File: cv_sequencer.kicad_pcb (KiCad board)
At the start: 4 copper layers, 111.3 x 22.4 mm, 110 parts, among them J1 4027_Connector_PicoBlade_3pos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, J10 3085_MiniJack_Thonk_Vert, J11 3085_MiniJack_Thonk_Vert, J12 3085_MiniJack_Thonk_Vert, J13 3085_MiniJack_Thonk_Vert, J2 4005_SWD_Header, J3 3086_Connector_Eurorack_Power, J4 3096_USBC_RA_SMD, J5 CV_OFFSET, J6 3085_MiniJack_Thonk_Vert, J7 3085_MiniJack_Thonk_Vert, J8 3085_MiniJack_Thonk_Vert, J9 3085_MiniJack_Thonk_Vert, SW1 RST, SW2 BOOTSEL, U1 3097_TFT_Display_SPI, U2 4002_RP2040, U3 4015_Adjustable_Reg_500mA_SOT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, U4 4015_Adjustable_Reg_500mA_SOT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, U5 4014_Voltage_Reference_5V_SOT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, U6 4001_MCP48FEB24_DAC, U7 3099_TL074CPW_SMD, U8 3099_TL074CPW_SMD, Y1 4004-Crystal-12MHz_GND24

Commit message: Made minor tweaks, started routing of board
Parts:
- added R31: 4030_Resistor_SMD_220_0.125W_1%, Shulltronics_Generics:RES-0402, B.Cu at (137.6, 77.9)
- added R32: 4008_Resistor_SMD_10k_0.125W_1%, Shulltronics_Generics:RES-0402, B.Cu at (145.3, 70.5)
- added R33: 4030_Resistor_SMD_220_0.125W_1%, Shulltronics_Generics:RES-0402, B.Cu at (136.4, 77.9)
- added U9: 4028_OptoIsolator_TLP290, Shulltronics_Opto:4028_OptoIsolator_TLP290_SOP-4, B.Cu at (140.8, 74.9)
- C13, C15, C16, C17: value 4013_Capacitor_1u_16V_0402 -> 4035_Capacitor_2u2_25V_0402
- C20, C21: value 3088_Capacitor_10u_50V_SMD -> 4031_Capacitor_10u_35V_SMD
- J1: value 4027_Connector_PicoBlade_3pos_Vert_THT -> 4029_Connector_PicoBlade_4pos_Vert_THT; footprint Shulltronics_Connectors:4027_PicoBlade_3pos_Vert_THT -> Shulltronics_Connectors:4029_PicoBlade_4pos_Vert_THT
- R10: value 4020_Resistor_SMD_180k_0.125W_1% -> 4033_Resistor_SMD_18k_0.125W_1%
- R11, R9: value 4019_Resistor_SMD_270k_0.125W_1% -> 4016_Resistor_SMD_27k_0.125W_1%
- R12: value 4018_Resistor_SMD_82k_0.125W_1% -> 4034_Resistor_SMD_8k2_0.125W_1%
- TP11, TP12, TP15, TP16, TP18: moved to F.Cu
- U3, U4: value 4015_Adjustable_Reg_500mA_SOT-23-5 -> 4032_Adjustable_Reg_200mA_SOT-23-5
- moved TP11 95.7 mm to (138.5, 85.4), turned to 0 degrees
- moved TP15 89.5 mm to (131.2, 85.3), turned to 0 degrees
- moved TP12 89.3 mm to (141.6, 85.4), turned to 0 degrees
- moved TP16 89.0 mm to (128.1, 85.3), turned to 0 degrees
- moved TP18 88.6 mm to (125.0, 85.3), turned to 0 degrees
- moved TP28 41.1 mm to (165.6, 85.3)
- moved TP29 39.7 mm to (168.7, 85.3)
- moved R24 37.8 mm to (172.8, 75.1)
- moved R27 37.3 mm to (172.8, 77.6), turned to 180 degrees
- moved R23 35.4 mm to (172.8, 76.4), turned to 0 degrees
- moved R1 35.2 mm to (146.6, 70.5), turned to -90 degrees
- moved R28 35.0 mm to (172.8, 73.8), turned to 0 degrees
- moved TP19 31.2 mm to (168.9, 66.0)
- moved TP20 31.2 mm to (175.1, 66.0)
- moved TP22 28.0 mm to (165.8, 66.0)
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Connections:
- net Net-(J5-Pad2) renamed /IO Jacks/CVx_REF
- C22 pad 2: /IO Jacks/5V3 -> /5V3
- C8 pad 2: /XOUT -> Net-(C8-Pad2)
- J1 pad 1: unconnected-(J1-Pad1) -> /MIDI_SNK
- J1 pad 2: unconnected-(J1-Pad2) -> /MIDI_SRC
- J1 pad 3: unconnected-(J1-Pad3) -> /UART_TX
- R10 pad 1: GND -> Net-(R9-Pad2)
- R10 pad 2: Net-(R10-Pad2) -> GND
- R11 pad 1: Net-(R11-Pad1) -> /5V3
- R11 pad 2: /5V3 -> Net-(R11-Pad2)
- R12 pad 1: GND -> Net-(R11-Pad2)
- R12 pad 2: Net-(R11-Pad1) -> GND
- R4 pad 1: /XOUT -> Net-(C8-Pad2)
- R4 pad 2: Net-(R4-Pad2) -> /XOUT
- R9 pad 1: Net-(R10-Pad2) -> VCC
- R9 pad 2: VCC -> Net-(R9-Pad2)
- U2 pad 21: Net-(R4-Pad2) -> /XOUT
- U3 pad 4: Net-(R10-Pad2) -> Net-(R9-Pad2)
- U4 pad 4: Net-(R11-Pad1) -> Net-(R11-Pad2)
- U5 pad 3: /IO Jacks/5V3 -> /5V3
- U6 pad 2: /IO Jacks/5V3 -> /5V3
- Y1 pad 3: /XOUT -> Net-(C8-Pad2)
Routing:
- net VSS: track 0.00 -> 105.3 mm, vias 0 -> 3
- net VDD: track 0.00 -> 100.9 mm, vias 0 -> 3
- net /~{RESET}: track 0.00 -> 47.5 mm, vias 0 -> 4
- net /IO Jacks/TRIG0: track 0.00 -> 35.3 mm
- net /IO Jacks/CV3_OUT: track 0.00 -> 32.3 mm
- net /IO Jacks/CV0_OUT: track 0.00 -> 26.9 mm
- net GND: track 0.00 -> 24.5 mm, vias 0 -> 28
- net /SWCLK: track 0.00 -> 23.8 mm, vias 0 -> 2
- net /SWDIO: track 0.00 -> 22.6 mm, vias 0 -> 2
- net /IO Jacks/DAC_VOUT3: track 0.00 -> 21.5 mm, vias 0 -> 2
- net /IO Jacks/DAC_VOUT1: track 0.00 -> 18.6 mm, vias 0 -> 2
- net /IO Jacks/TRIG1: track 0.00 -> 18.4 mm
- net VCC: track 0.00 -> 16.6 mm, vias 0 -> 15
- net /IO Jacks/DAC_VOUT2: track 0.00 -> 16.0 mm, vias 0 -> 2
- net /IO Jacks/DAC_VOUT0: track 0.00 -> 14.3 mm, vias 0 -> 2
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- added copper zone on B.Cu, net GND
- added copper zone on In2.Cu, net GND
- added copper zone on F.Cu, net VCC
- added copper zone on B.Cu, net VDD
- added copper zone on B.Cu, net VSS

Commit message: some more routing
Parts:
- removed TP1: ENC_BTN, Shulltronics_Generics:TestPoint_Pad_D2.0mm
- removed TP2: LCD/SD_SCK, Shulltronics_Generics:TestPoint_Pad_D2.0mm
- removed TP21: DAC_VOUT0, Shulltronics_Generics:TestPoint_Pad_D2.0mm
- removed TP25: DAC_VOUT2, Shulltronics_Generics:TestPoint_Pad_D2.0mm
- removed TP26: DAC_VOUT3, Shulltronics_Generics:TestPoint_Pad_D2.0mm
- removed TP29: TRIG1, Shulltronics_Generics:TestPoint_Pad_D2.0mm
- removed TP3: SD_SDO, Shulltronics_Generics:TestPoint_Pad_D2.0mm
- removed TP30: TRIG2, Shulltronics_Generics:TestPoint_Pad_D2.0mm
- removed TP31: TRIG3, Shulltronics_Generics:TestPoint_Pad_D2.0mm
- removed TP4: LCD/SD_SDI, Shulltronics_Generics:TestPoint_Pad_D2.0mm
- removed TP5: LCD_CS, Shulltronics_Generics:TestPoint_Pad_D2.0mm
- removed TP6: LCD_RST, Shulltronics_Generics:TestPoint_Pad_D2.0mm
- removed TP7: LCD_DC, Shulltronics_Generics:TestPoint_Pad_D2.0mm
- removed TP8: SD_CS, Shulltronics_Generics:TestPoint_Pad_D2.0mm
- moved TP24 26.5 mm to (174.5, 66.0)
- moved TP23 9.91 mm to (162.1, 66.0)
- moved TP20 9.91 mm to (165.2, 66.0)
- moved R17 9.02 mm to (193.9, 80.5), turned to 180 degrees
- moved R18 7.19 mm to (196.5, 72.3)
- moved R22 7.19 mm to (194.3, 72.3)
- moved R21 6.67 mm to (193.9, 79.2), turned to 0 degrees
- moved C10 3.30 mm to (155.3, 71.1), turned to 90 degrees
- moved TP28 3.25 mm to (162.3, 85.3)
- moved TP19 2.49 mm to (171.4, 66.0)
- moved TP22 2.49 mm to (168.3, 66.0)
- moved R2 1.37 mm to (154.9, 66.8)
- moved R3 1.27 mm to (154.9, 68.2)
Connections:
- U2 pad 38: /IO_TRIG0 -> /IO_TRIG3
- U2 pad 41: /IO_TRIG3 -> /IO_TRIG0
- U8 pad 10: /IO Jacks/TRIG2 -> /IO Jacks/TRIG3
- U8 pad 12: /IO Jacks/TRIG3 -> /IO Jacks/TRIG2
- U8 pad 13: /IO Jacks/TRIG3_FB -> /IO Jacks/TRIG2_FB
- U8 pad 14: /IO Jacks/TRIG3_FB -> /IO Jacks/TRIG2_FB
- U8 pad 8: /IO Jacks/TRIG2_FB -> /IO Jacks/TRIG3_FB
- U8 pad 9: /IO Jacks/TRIG2_FB -> /IO Jacks/TRIG3_FB
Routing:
- net /5V3: track 5.44 -> 72.8 mm, vias 0 -> 2
- net /IO_TRIG0: track 0.00 -> 46.3 mm, vias 0 -> 3
- net /IO_TRIG3: track 2.64 -> 45.7 mm, vias 0 -> 2
- net /IO_TRIG2: track 1.67 -> 43.5 mm, vias 0 -> 3
- net /ENC_1: track 0.00 -> 40.3 mm, vias 0 -> 2
- net /ENC_BTN: track 5.93 -> 41.4 mm, vias 0 -> 3
- net /IO_TRIG1: track 0.00 -> 35.4 mm, vias 0 -> 2
- net /ENC_0: track 0.00 -> 34.9 mm, vias 0 -> 2
- net /SD_CS: track 0.00 -> 22.7 mm, vias 0 -> 2
- net /LCD_DC: track 0.00 -> 22.0 mm, vias 0 -> 1
- net /LCD_RST: track 0.00 -> 17.3 mm, vias 0 -> 1
- net /IO_SDI: track 6.20 -> 22.9 mm, vias 2 -> 4
- net /VREG_1V2: track 3.00 -> 18.9 mm, vias 0 -> 3
- net /IO_SDO: track 5.94 -> 20.7 mm, vias 0 -> 2
- net /LCD_CS: track 0.00 -> 13.5 mm
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
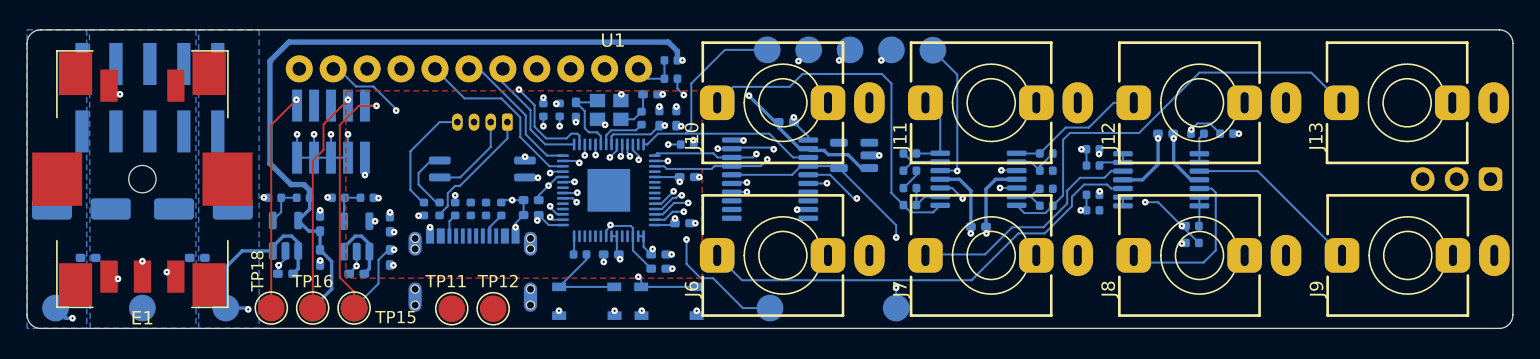
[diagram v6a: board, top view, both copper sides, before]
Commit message: Added a few 0 ohm options, finished routing, ordered board!
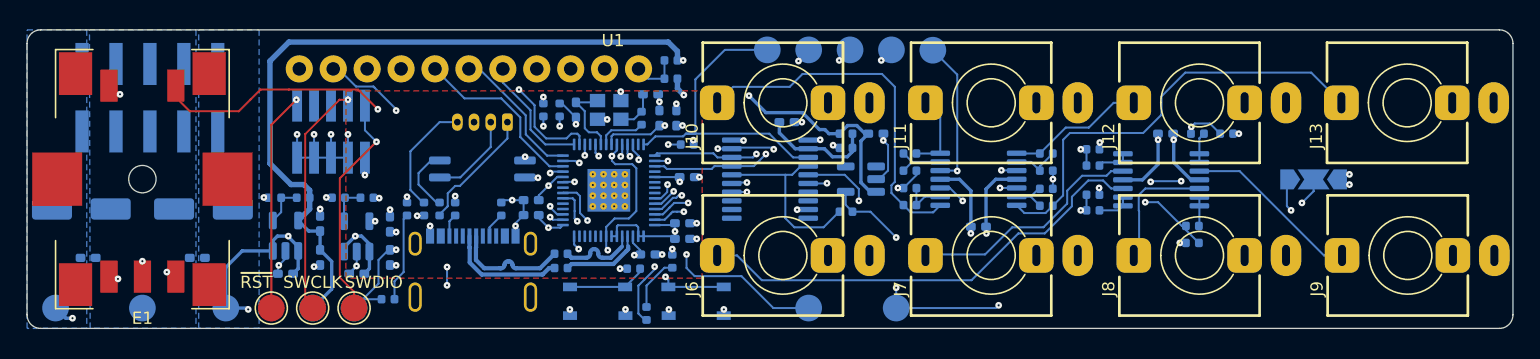
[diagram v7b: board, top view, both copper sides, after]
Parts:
- removed TP11: USB_D-, Shulltronics_Generics:TestPoint_Pad_D2.0mm
- removed TP12: USB_D+, Shulltronics_Generics:TestPoint_Pad_D2.0mm
- added L1: Shulltronics_Logo, Shulltronics_Generics:Shulltronics_Logo, B.Cu at (205.4, 66.4)
- added R34: 4038_Resistor_SMD_100_0.125W_1%, Shulltronics_Generics:RES-0402, B.Cu at (135.1, 77.9)
- added R35: 4038_Resistor_SMD_100_0.125W_1%, Shulltronics_Generics:RES-0402, B.Cu at (155.0, 81.8)
- added R36: 4021_Resistor_SMD_Jumper, Shulltronics_Generics:RES-0402, B.Cu at (168.0, 72.3)
- added R37: JMP, Shulltronics_Generics:RES-0402, B.Cu at (168.0, 78.1)
- added R38: DNP, Shulltronics_Generics:RES-0402, B.Cu at (168.0, 73.4)
- added U10: PWR, Shulltronics_Generics:LED_0402, B.Cu at (133.7, 84.7)
- added U11: STAT, Shulltronics_Generics:LED_0402, B.Cu at (153.1, 85.8)
- C3: value 3089_Capacitor_100n_16V_0402 -> 3089_Capacitor_100n_16V_SMD
- J1: value 4029_Connector_PicoBlade_4pos_Vert_THT -> :MIDI_IO
- J2: value 4005_SWD_Header -> SWD
- J5: footprint Shulltronics_Connectors:3046_Header_3pos_2.54mm -> Shulltronics_Generics:SMD_SolderJumper-3
- SW2: value BOOTSEL -> BOOT
- TP19: value DAC_SDI -> SDI
- TP20: value DAC_SCK -> SCK
- TP22: value DAC_SDO -> SDO
- TP23: value DAC_~{CS} -> ~{CS}
- TP24: value DAC_VOUT1 -> DAC1
- TP27: value VREF_5V0 -> 5V0
- moved C3 16.5 mm to (163.6, 71.4), turned to 180 degrees
- moved J5 10.7 mm to (203.0, 75.7), turned to 180 degrees
- moved R7 8.07 mm to (146.7, 82.3), turned to 0 degrees
- moved C22 6.76 mm to (170.2, 72.3)
- moved R6 6.54 mm to (146.7, 81.3), turned to 0 degrees
- moved R5 4.15 mm to (152.1, 82.4)
- moved TP28 2.90 mm to (165.2, 85.3)
- moved C2 2.13 mm to (155.8, 80.2)
- moved SW1 2.03 mm to (156.8, 84.8)
- moved U5 1.85 mm to (169.1, 75.7)
- moved C12 1.34 mm to (153.2, 81.3)
- moved SW2 0.81 mm to (149.4, 84.9)
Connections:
- C3 pad 2: VCC -> /IO Jacks/DAC_VDD
- U2 pad 37: unconnected-(U2-Pad37) -> /STAT_LED
- U6 pad 16: /IO Jacks/VREF_5V0 -> Net-(U6-Pad16)
- U6 pad 2: /5V3 -> /IO Jacks/DAC_VDD
- U6 pad 4: /IO Jacks/VREF_5V0 -> Net-(U6-Pad16)
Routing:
- net /~{RESET}: track 35.5 -> 74.4 mm, vias 4 -> 6
- net VCC: track 23.6 -> 59.7 mm
- net /IO Jacks/CVx_REF: track 1.71 -> 37.5 mm, vias 0 -> 5
- net /SWCLK: track 18.1 -> 47.5 mm
- net /IO Jacks/VREF_5V0: track 20.6 -> 47.6 mm, vias 2 -> 4
- net /SWDIO: track 19.4 -> 46.0 mm
- net Net-(U6-Pad16): track 0.00 -> 14.1 mm
- net /STAT_LED: track 0.00 -> 13.1 mm, vias 0 -> 2
- net /USB_D+: track 0.00 -> 8.94 mm
- net /USB_D-: track 0.00 -> 8.92 mm
- net /IO Jacks/DAC_VDD: track 0.00 -> 8.52 mm
- net Net-(R34-Pad1): track 0.00 -> 6.66 mm
- net /D-: track 0.00 -> 6.12 mm
- net /D+: track 0.00 -> 6.07 mm
- net VDD: track 109.1 -> 114.2 mm, vias 3 -> 5
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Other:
- board text added: "cv_binary_sequencer rev 0.1"
- board text added: "rev 0.1: Ran DRC, only issues are with courtyard overlaps with test pads. All OK. Hopefully this works somewhat!"

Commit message: updated jack and encoder footprints with user drawing layer
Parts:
- J10, J11, J12, J13, J6, J7, J8, J9: value 3085_MiniJack_Thonk_Vert -> PJ398SM
